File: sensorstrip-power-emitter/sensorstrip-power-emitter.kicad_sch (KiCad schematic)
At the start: 11 parts, among them J1 USB_C_Receptacle_PowerOnly, J2 Conn_01x02_MountingPin, SW1 SW_DPDT_x2

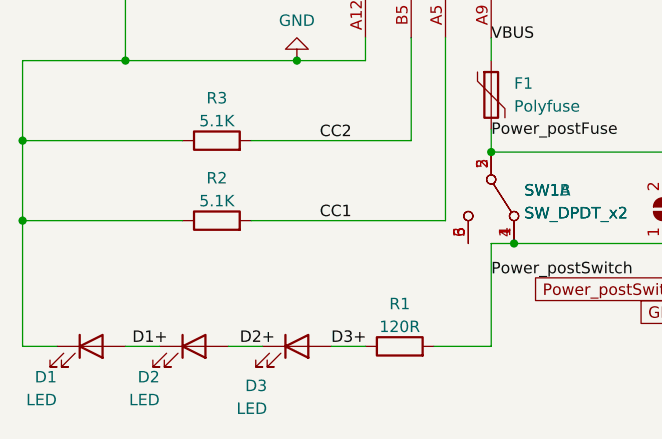
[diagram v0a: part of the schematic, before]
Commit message: Rename sender / receiver boards to power-emitter and emitter
...hopefully this is clearer

Also some tidying of older boards
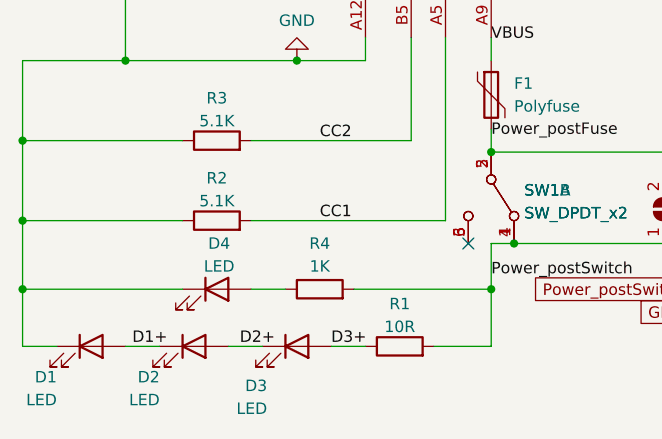
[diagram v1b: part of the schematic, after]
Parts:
- added D4: LED, LED_SMD:LED_0603_1608Metric_Pad1.05x0.95mm_HandSolder, symbol Device:LED
- added R4: 1K, Resistor_SMD:R_0603_1608Metric_Pad0.98x0.95mm_HandSolder, symbol Device:R
- J2: footprint Connector_Molex:Molex_PicoBlade_53261-0271_1x02-1MP_P1.25mm_Horizontal -> sensorstrip:Molex_Picoblade_53261-0271-Hybrid
- R1: value 120R -> 10R
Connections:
- net GND: now also D4.1 (K)
- net Power_postSwitch: now also R4.2
- new net: D4.2 (A), R4.1
- no-connect marks 0 -> 1
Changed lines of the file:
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@@
+	)
+	(junction
+		(at 115.57 85.09)
+		(diameter 0)
+		(color 0 0 0 0)
 	)
 	(junction
@@
 	)
 	(junction
+		(at 63.5 85.09)
+		(diameter 0)
+		(color 0 0 0 0)
+	)
+	(junction
 		(at 63.5 68.58)
 		(diameter 0)
@@
 		(color 0 0 0 0)
 	)
+	(no_connect
+		(at 113.03 80.01)
+	)
 	(wire
 		(pts
@@
 	(wire
 		(pts
+			(xy 100.33 85.09) (xy 115.57 85.09)
+		)
+		(stroke
+			(width 0)
+			(type default)
+		)
+	)
+	(wire
+		(pts
 			(xy 88.9 68.58) (xy 106.68 68.58)
 		)
@@
 	(wire
 		(pts
-			(xy 63.5 77.47) (xy 63.5 91.44)
+			(xy 63.5 77.47) (xy 63.5 85.09)
 		)
 		(stroke
@@
 	(wire
 		(pts
+			(xy 63.5 85.09) (xy 63.5 91.44)
+		)
+		(stroke
+			(width 0)
+			(type default)
+		)
+	)
+	(wire
+		(pts
 			(xy 134.62 80.01) (xy 118.11 80.01)
 		)
@@
 	(wire
 		(pts
+			(xy 88.9 85.09) (xy 92.71 85.09)
+		)
+		(stroke
+			(width 0)
+			(type default)
+		)
+	)
+	(wire
+		(pts
 			(xy 63.5 68.58) (xy 63.5 77.47)
 		)
@@
 	(wire
 		(pts
+			(xy 115.57 85.09) (xy 115.57 91.44)
+		)
+		(stroke
+			(width 0)
+			(type default)
+		)
+	)
+	(wire
+		(pts
 			(xy 106.68 68.58) (xy 106.68 57.15)
 		)
@@
 	(wire
 		(pts
+			(xy 63.5 85.09) (xy 81.28 85.09)
+		)
+		(stroke
+			(width 0)
+			(type default)
+		)
+	)
+	(wire
+		(pts
 			(xy 115.57 67.31) (xy 115.57 69.85)
 		)
@@
 	(wire
 		(pts
-			(xy 115.57 80.01) (xy 115.57 91.44)
+			(xy 115.57 80.01) (xy 115.57 85.09)
 		)
 		(stroke
@@
 			)
 		)
-		(property "Footprint" "Connector_Molex:Molex_PicoBlade_53261-0271_1x02-1MP_P1.25mm_Horizontal"
+		(property "Footprint" "sensorstrip:Molex_Picoblade_53261-0271-Hybrid"
 			(at 143.51 85.09 0)
 			(effects
@@
 	)
 	(symbol
+		(lib_id "Device:R")
+		(at 96.52 85.09 90)
+		(unit 1)
+		(exclude_from_sim no)
+		(in_bom yes)
+		(on_board yes)
+		(dnp no)
+		(property "Reference" "R4"
+			(at 96.52 80.01 90)
+			(effects
+				(font
+					(size 1.27 1.27)
+				)
+			)
+		)
+		(property "Value" "1K"
+			(at 96.52 82.55 90)
+			(effects
+				(font
+					(size 1.27 1.27)
+				)
+			)
+		)
+		(property "Footprint" "Resistor_SMD:R_0603_1608Metric_Pad0.98x0.95mm_HandSolder"
+			(at 96.52 86.868 90)
+			(effects
+				(font
+					(size 1.27 1.27)
+				)
+				(hide yes)
+			)
+		)
+		(property "Datasheet" "~"
+			(at 96.52 85.09 0)
+			(effects
+				(font
+					(size 1.27 1.27)
+				)
+				(hide yes)
+			)
+		)
+		(property "Description" ""
+			(at 96.52 85.09 0)
+			(effects
+				(font
+					(size 1.27 1.27)
+				)
+				(hide yes)
+			)
+		)
+		(pin "1"
+		)
+		(pin "2"
+		)
+		(instances
+			(project "sensorstrip-power-emitter"
+				(path "/de367d23-fe77-4b45-8815-68113c5ee5ff"
+					(reference "R4")
+					(unit 1)
+				)
+			)
+		)
+	)
+	(symbol
+		(lib_id "Device:LED")
+		(at 85.09 85.09 0)
+		(unit 1)
+		(exclude_from_sim no)
+		(in_bom yes)
+		(on_board yes)
+		(dnp no)
+		(property "Reference" "D4"
+			(at 85.344 80.01 0)
+			(effects
+				(font
+					(size 1.27 1.27)
+				)
+			)
+		)
+		(property "Value" "LED"
+			(at 85.344 82.55 0)
+			(effects
+				(font
+					(size 1.27 1.27)
+				)
+			)
+		)
+		(property "Footprint" "LED_SMD:LED_0603_1608Metric_Pad1.05x0.95mm_HandSolder"
+			(at 85.09 85.09 0)
+			(effects
+				(font
+					(size 1.27 1.27)
+				)
+				(hide yes)
+			)
+		)
+		(property "Datasheet" "~"
+			(at 85.09 85.09 0)
+			(effects
+				(font
+					(size 1.27 1.27)
+				)
+				(hide yes)
+			)
+		)
+		(property "Description" "Light emitting diode"
+			(at 85.09 85.09 0)
+			(effects
+				(font
+					(size 1.27 1.27)
+				)
+				(hide yes)
+			)
+		)
+		(pin "1"
+		)
+		(pin "2"
+		)
+		(instances
+			(project "sensorstrip-power-emitter"
+				(path "/de367d23-fe77-4b45-8815-68113c5ee5ff"
+					(reference "D4")
+					(unit 1)
+				)
+			)
+		)
+	)
+	(symbol
 		(lib_id "sensorstrip:USB_C_Receptacle_PowerOnly")
 		(at 104.14 41.91 270)
@@
 			)
 		)
-		(property "Value" "120R"
+		(property "Value" "10R"
 			(at 105.41 89.2611 90)
 			(effects
